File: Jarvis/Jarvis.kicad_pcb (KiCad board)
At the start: 4 copper layers, 30 x 50 mm, 163 parts, among them IC1 ADP1607, IC2 MAX-8Q, IC3 MPU-9250, IC4 STM32F411CxUx, IC5 Si4460, IC6 MS5611-01BA03, IC7 S25FL127S, J1 PYRO, J2 PWR, J3 ARM, J4 MICROUSB, P1 SMA, P2 SMA, P3 SWD_TC, Q1 PFET, Q2 PFET, Q3 PFET, Q4 NFET, Q5 NFET, Q6 NFET, Q7 NFET, Y1 26MHz, Y2 30MHz

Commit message: Continued Layout
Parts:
- removed TP1, TP10, TP11, TP12, TP13, TP14, TP15, TP16, TP17, TP18, TP19, TP2, TP20, TP21, TP22, TP23, TP24, TP25, TP26, TP27, TP28, TP29, TP3, TP30, TP31, TP32, TP33, TP34, TP35, TP36, TP37, TP38, TP39, TP4, TP40, TP41, TP42, TP43, TP44, TP45, TP46, TP47, TP48, TP5, TP6, TP7, TP8, TP9: TESTPAD, agg:TESTPAD
- added C29: 100nF, agg:0402-L, F.Cu at (113.9, 101.6)
- added REF**: BMI-S-201-F, Library:BMI-S-201-F, F.Cu at (99.0, 80.7)
- C16: footprint agg:0603-L -> agg:0402-L
- moved C10 156.7 mm to (90.0, 101.3), turned to 0 degrees
- moved C11 150.6 mm to (89.0, 96.3), turned to 0 degrees
- moved C7 137.8 mm to (103.5, 106.8), turned to 270 degrees
- moved C9 132.2 mm to (95.0, 106.0), turned to 225 degrees
- moved FB2 130.9 mm to (89.0, 94.0)
- moved C19 130.6 mm to (97.9, 95.3), turned to 270 degrees
- moved C31 129.6 mm to (89.6, 110.6), turned to 180 degrees
- moved C18 128.4 mm to (94.4, 105.4), turned to 225 degrees
- moved C36 125.6 mm to (101.8, 88.1)
- moved C33 124.3 mm to (103.4, 90.5), turned to 270 degrees
- moved C8 123.7 mm to (103.1, 105.5), turned to 180 degrees
- moved C1 123.7 mm to (97.0, 90.1)
- moved C21 122.6 mm to (106.3, 104.6), turned to 180 degrees
- moved C37 122.5 mm to (102.2, 112.0)
- moved C15 122.4 mm to (86.7, 99.3), turned to 180 degrees
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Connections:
- IC4 pad 20: Net-(IC4-Pad20) -> /FLASH_RST
- IC7 pad 7: Net-(IC7-Pad7) -> /FLASH_RST
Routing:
- net 3v3: track 14.2 -> 57.7 mm, vias 6 -> 20
- net /SPI1_MOSI: track 0.00 -> 31.9 mm, vias 0 -> 3
- net /SPI1_NSS1_FLASH: track 0.00 -> 29.8 mm, vias 0 -> 2
- net /SPI1_NSS2_RADIO: track 0.00 -> 25.8 mm, vias 0 -> 2
- net /FLASH_RST: track 0.00 -> 25.3 mm, vias 0 -> 4
- net /SPI1_SCK: track 0.00 -> 22.1 mm, vias 0 -> 3
- net /SPI1_MISO: track 0.00 -> 19.2 mm, vias 0 -> 3
- net GND: track 0.00 -> 16.7 mm
- net /SPI2_MISO: track 0.00 -> 13.9 mm, vias 0 -> 2
- net /I2C1_SCL: track 3.90 -> 14.8 mm, vias 0 -> 2
- net /Radio_nIRQ: track 0.00 -> 9.41 mm
- net /USB_OTG_DP: track 0.00 -> 9.02 mm
- net /PYRO1_S: track 0.80 -> 9.77 mm, vias 0 -> 2
- net /USB_OTG_DM: track 0.00 -> 8.96 mm
- net /GPS_RST: track 0.00 -> 8.83 mm
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- added copper zone on F.Cu, net GND

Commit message: Continued PCB
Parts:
- moved R28 17.0 mm to (107.5, 106.7)
- moved R27 16.5 mm to (108.3, 106.7), turned to 90 degrees
- moved C17 0.64 mm to (97.1, 95.3), turned to 90 degrees
- moved C12 0.57 mm to (96.3, 95.3), turned to 90 degrees
- moved C1 0.40 mm to (97.0, 90.5)
- moved FB1 0.40 mm to (87.5, 94.0), turned to 0 degrees
- moved FB2 0.40 mm to (89.4, 94.0), turned to 180 degrees
- moved IC2 0.40 mm to (95.6, 82.8)
- moved C15 0.35 mm to (86.7, 99.0)
- moved C37 0.15 mm to (102.2, 111.8)
- moved C20 0.10 mm to (105.7, 100.8)
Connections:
- IC4 pad 2: /STAT_WRN -> /STAT_HBT
- IC4 pad 3: /STAT_HBT -> /STAT_WRN
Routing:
- net GND: track 16.7 -> 74.1 mm, vias 0 -> 13
- net /PYRO1_S: track 9.77 -> 44.0 mm
- net /PYRO2_S: track 4.99 -> 38.3 mm
- net /~RST: track 3.87 -> 34.5 mm
- net /PYRO3_S: track 4.14 -> 31.1 mm
- net /USART1_TX: track 3.22 -> 19.7 mm, vias 0 -> 2
- net /BATT_MON: track 0.87 -> 16.5 mm, vias 0 -> 2
- net /SPI2_NSS1_MPU: track 0.93 -> 15.9 mm, vias 0 -> 2
- net /STAT_WRN: track 2.36 -> 17.2 mm, vias 1 -> 2
- net /USART1_RX: track 4.90 -> 18.5 mm, vias 0 -> 2
- net /BEEPER: track 3.18 -> 16.0 mm
- net /SPI2_SCK: track 1.19 -> 12.2 mm, vias 1 -> 2
- net /PYRO1_F: track 3.57 -> 13.7 mm, vias 1 -> 2
- net /STAT_HBT: track 3.17 -> 12.5 mm, vias 1 -> 2
- net Net-(IC2-Pad11): track 0.00 -> 8.16 mm
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- added copper zone on B.Cu, net GND
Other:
- rule trace_min: 0.2 -> 0.18

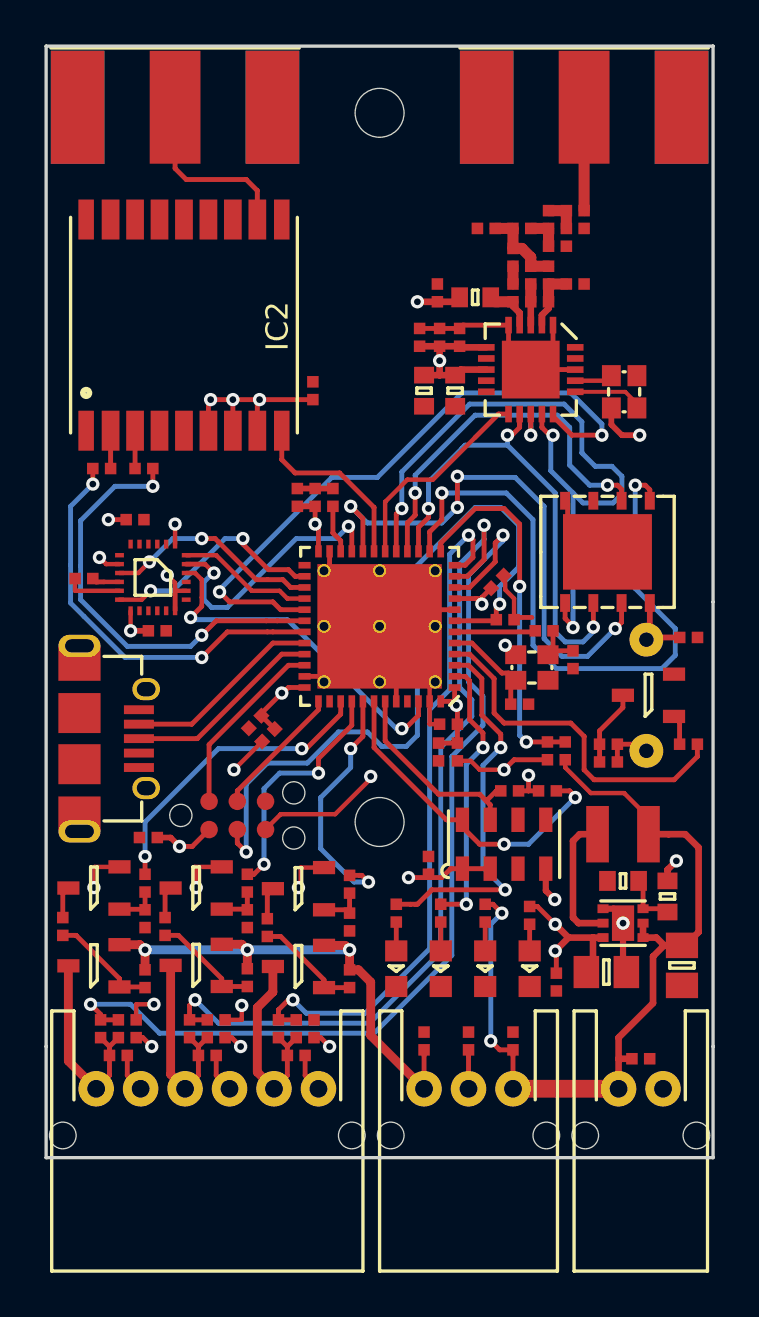
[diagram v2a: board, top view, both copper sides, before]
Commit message: Ready to Check Footprints
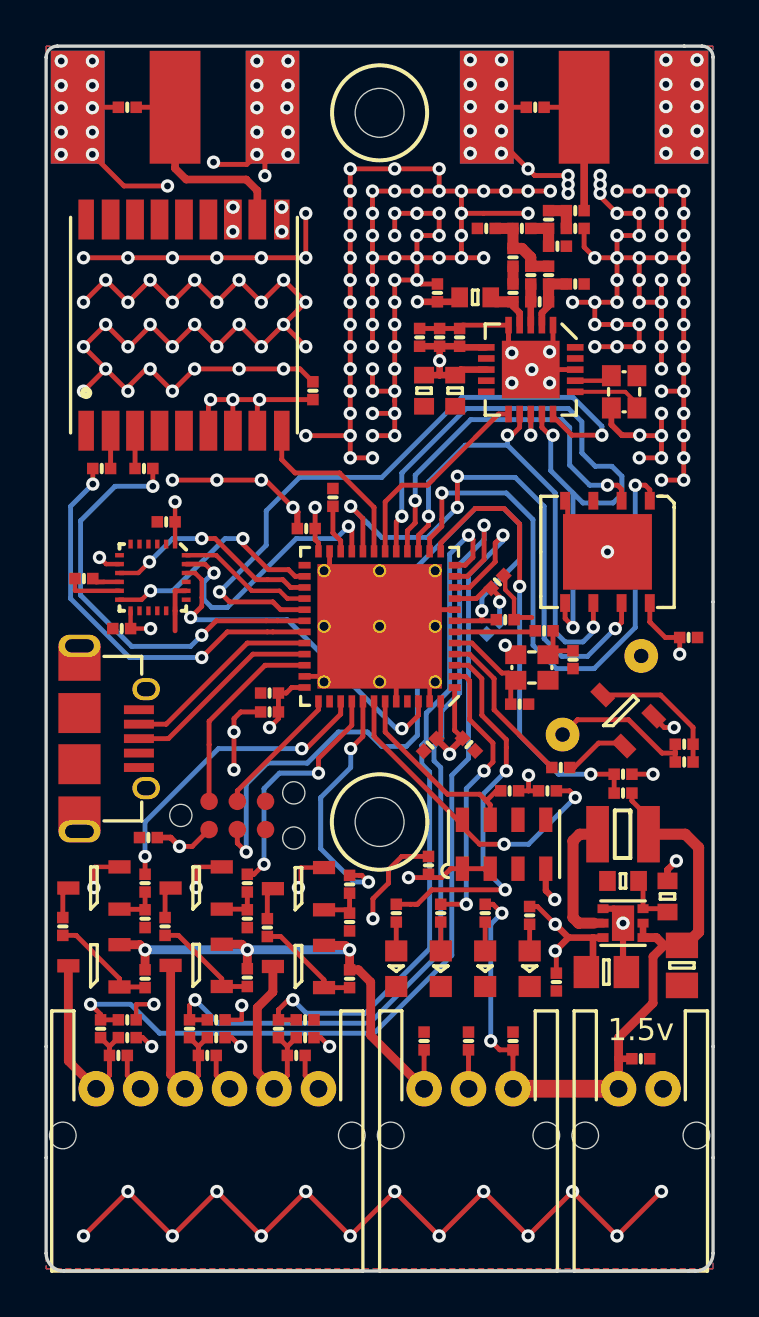
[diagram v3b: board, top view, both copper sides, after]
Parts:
- removed C18: 100nF, agg:0402-L
- added D11: ESD_DIODE, agg:0402-L, F.Cu at (88.7, 77.8)
- added D12: ESD_DIODE, agg:0402-L, F.Cu at (107.0, 77.8)
- added G***: LOGO, Library:Logo, B.Cu at (100.0, 93.8)
- C16: moved to B.Cu
- moved C17 9.04 mm to (105.3, 99.1), turned to 45 degrees
- moved C7 8.64 mm to (95.0, 105.0), turned to 180 degrees
- moved R34 5.84 mm to (108.2, 107.5), turned to 0 degrees
- moved R28 3.56 mm to (111.0, 107.8), turned to 0 degrees
- moved R29 3.50 mm to (113.7, 106.4), turned to 0 degrees
- moved R33 3.50 mm to (113.7, 107.2), turned to 0 degrees
- moved R27 3.22 mm to (111.0, 108.6), turned to 180 degrees
- moved C16 2.07 mm to (105.1, 101.2), turned to 225 degrees
- moved LS1 2.00 mm to (110.0, 104.2), turned to 135 degrees
- moved C9 1.90 mm to (95.0, 104.1), turned to 180 degrees
- moved C10 1.60 mm to (88.4, 101.2), turned to 180 degrees
- moved Q7 1.48 mm to (110.8, 105.0), turned to 135 degrees
- moved C12 1.46 mm to (96.7, 96.7), turned to 180 degrees
- moved C13 1.41 mm to (104.0, 106.4), turned to 315 degrees
- moved C11 1.40 mm to (90.4, 96.4), turned to 180 degrees
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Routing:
- net GND: track 74.1 -> 352.5 mm, vias 13 -> 240
- net /BEEPER: track 16.0 -> 7.46 mm
- net Net-(LS1-Pad2): track 2.23 -> 6.77 mm
- net /BATT_MON: track 16.5 -> 20.2 mm
- net VBATT: track 38.9 -> 35.3 mm
- net /SPI1_NSS1_FLASH: track 29.8 -> 26.5 mm
- net Net-(Q7-Pad3): track 3.43 -> 6.22 mm
- net 3v3: track 59.5 -> 61.7 mm
- net Net-(D12-Pad1): track 5.78 -> 7.58 mm
- net Net-(D11-Pad2): track 8.16 -> 9.91 mm
- net Net-(Q7-Pad1): track 1.35 -> 2.95 mm
- net /SPI1_MISO: track 19.2 -> 18.4 mm
- net /~RST: track 34.5 -> 33.7 mm
- net /SPI1_NSS2_RADIO: track 28.9 -> 29.5 mm
- net /SWDIO: track 8.32 -> 8.94 mm
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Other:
- board size 30 x 50 mm -> 30 x 55.1 mm
- board text added: "1.5v"
- board text added: "GND"
- board text added: "GPS"
- board text added: "Jarvis Flight Computer By Matthew Coates"
- board text added: "LED"
- board text added: "M2"
- board text added: "PYRO1"
- board text added: "PYRO2"
- board text added: "PYRO3"
- board text added: "RADIO"
- board text added: "SIN"
- board text added: "SOUT"
- board text added: "USB"
- board text added: "VBATT"

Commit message: Finished PCB
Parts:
- moved C1 6.17 mm to (91.9, 94.0), turned to 180 degrees
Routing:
- net GND: track 352.5 -> 120.7 mm, vias 240 -> 155
- net 3v3: track 61.7 -> 58.7 mm, vias 22 -> 20
- net /SPI1_MOSI: track 31.7 -> 29.9 mm
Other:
- board text added: "1.6v"
- board text removed: "1.5v"

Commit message: Finished ground station
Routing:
- net GND: track 120.7 -> 338.3 mm, vias 155 -> 168
- net Net-(D12-Pad1): track 7.58 -> 6.45 mm
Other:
- board text added: "Jarvis Flight Computer Matthew Coates"
- board text removed: "Jarvis Flight Computer By Matthew Coates"

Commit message: Checked all Footprints
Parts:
- IC7: footprint agg:WND008 -> agg:S25FL127S
- L1: footprint Inductors_NEOSID:Neosid_Inductor_SM-NE29_SMD1008 -> Library:VLF252012MT
- moved C29 6.85 mm to (113.7, 94.8), turned to 180 degrees
- moved IC7 0.47 mm to (110.7, 97.9)
- moved L1 0.07 mm to (111.0, 110.5)
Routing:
- net /SPI1_NSS1_FLASH: track 26.5 -> 7.04 mm, vias 2 -> 0
- net GND: track 338.3 -> 344.6 mm, vias 168 -> 169
- net /FLASH_RST: track 25.3 -> 21.0 mm
- net /SPI1_MOSI: track 29.9 -> 25.6 mm
- net /SPI1_SCK: track 22.1 -> 24.2 mm, vias 3 -> 2
- net /SPI1_NSS2_RADIO: track 29.6 -> 27.5 mm
- net /SPI1_MISO: track 18.4 -> 16.9 mm
- net 3v3: track 58.7 -> 57.8 mm
- net /Radio_nIRQ: track 9.41 -> 10.3 mm
- net VBATT: track 35.3 -> 35.9 mm

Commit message: All checked and panel completed
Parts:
- added TP15: TESTPAD, agg:TESTPAD, B.Cu at (86.0, 94.5)
- added TP19: TESTPAD, agg:TESTPAD, B.Cu at (87.6, 96.4)
- added TP23: TESTPAD, agg:TESTPAD, F.Cu at (94.7, 94.6)
- added TP27: TESTPAD, agg:TESTPAD, B.Cu at (90.2, 96.6)
- added TP28: TESTPAD, agg:TESTPAD, B.Cu at (93.6, 101.6)
- added TP30: TESTPAD, agg:TESTPAD, B.Cu at (88.4, 99.0)
- added TP31: TESTPAD, agg:TESTPAD, B.Cu at (95.0, 99.8)
- added TP32: TESTPAD, agg:TESTPAD, B.Cu at (88.8, 100.2)
- added TP33: TESTPAD, agg:TESTPAD, B.Cu at (108.2, 98.0)
- added TP36: TESTPAD, agg:TESTPAD, B.Cu at (110.6, 96.2)
- added TP37: TESTPAD, agg:TESTPAD, B.Cu at (107.5, 99.5)
- added TP39: TESTPAD, agg:TESTPAD, B.Cu at (111.0, 100.5)
- added TP43: TESTPAD, agg:TESTPAD, B.Cu at (99.9, 95.5)
- added TP44: TESTPAD, agg:TESTPAD, B.Cu at (102.1, 90.8)
- added TP49: TESTPAD, agg:TESTPAD, B.Cu at (114.0, 95.5)
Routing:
- net /SPI2_MOSI: track 6.13 -> 9.61 mm, vias 0 -> 1
- net /SPI1_MISO: track 16.9 -> 19.3 mm
- net /SPI1_NSS1_FLASH: track 7.04 -> 9.12 mm, vias 0 -> 1
- net /GPS_RST: track 8.32 -> 9.71 mm
- net /SPI1_MOSI: track 25.6 -> 26.9 mm
- net /MPU_IRQ: track 10.3 -> 11.5 mm
- net /SPI1_NSS2_RADIO: track 27.5 -> 28.6 mm
- net /FLASH_RST: track 21.0 -> 22.1 mm
- net /SPI2_SCK: track 12.2 -> 13.2 mm
- net /USART1_RX: track 18.4 -> 19.3 mm
- net /SPI1_SCK: track 24.2 -> 25.1 mm
- net /USART1_TX: track 19.5 -> 20.4 mm
- net /SPI2_NSS1_MPU: track 15.9 -> 16.7 mm
- net /SPI2_MISO: track 9.88 -> 10.6 mm
- net /Radio_nIRQ: track 10.3 -> 10.9 mm, vias 0 -> 1

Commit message: Modified tolerence
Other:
- rule trace_min: 0.18 -> 0.1524
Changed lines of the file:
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@@
     (links 308)
     (no_connects 0)
-    (area 84.924998 74.924999 115.075001 130.175002)
+    (area 81.675 72.611 117.344048 131.975)
     (thickness 1.6)
     (drawings 164)
@@
   (layers
     (0 F.Cu signal)
-    (1 In1.Cu power hide)
-    (2 In2.Cu power hide)
+    (1 In1.Cu power)
+    (2 In2.Cu power)
     (31 B.Cu signal)
     (32 B.Adhes user hide)
@@
     (zone_clearance 0.22)
     (zone_45_only no)
-    (trace_min 0.18)
+    (trace_min 0.1524)
     (segment_width 0.18)
     (edge_width 0.15)
@@
   )
   (zone (net 2) (net_name GND) (layer In1.Cu) (hatch edge 0.508)
-    (connect_pads (clearance 0.22))
-    (min_thickness 0.254)
-    (fill yes (arc_segments 32) (thermal_gap 0.25) (thermal_bridge_width 0.3))
+    (connect_pads (clearance 0.26))
+    (min_thickness 0.26)
+    (fill yes (arc_segments 32) (thermal_gap 0.26) (thermal_bridge_width 0.3))
     (polygon
       (pts
@@
   )
   (zone (net 1) (net_name 3v3) (layer In2.Cu) (hatch edge 0.508)
-    (connect_pads (clearance 0.22))
-    (min_thickness 0.254)
-    (fill yes (arc_segments 32) (thermal_gap 0.25) (thermal_bridge_width 0.3))
+    (connect_pads (clearance 0.26))
+    (min_thickness 0.26)
+    (fill yes (arc_segments 32) (thermal_gap 0.26) (thermal_bridge_width 0.3))
     (polygon
       (pts
